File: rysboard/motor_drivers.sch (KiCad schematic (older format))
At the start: 36 parts, among them J2 Motor L, J3 Motor R, Q11 NST847BDP6T5G, Q8 DMP3036SSD-13, U1 L6470, U2 L6470, U5 74HC2G00

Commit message: fixed some bugs. Input protection done. Started implementing 5V Regulator
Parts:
- renumbered Q11 to Q3, Q8 to Q5
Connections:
- net GND: now also Q3.4 (E2); no longer Q3.1 (E1)
- net at R68.1: now also Q3.5 (B2); no longer Q3.2 (B1)
- net at Q5.4 (G2), R69.2: now also Q3.3 (C2); no longer Q3.6 (C1)
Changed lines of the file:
@@
 Connection ~ 3850 950
 $Comp
-L rysboard:NST847BDP6T5G Q11
-U 1 1 603A44DC
+L rysboard:NST847BDP6T5G Q3
+U 2 1 603A44DC
 P 2400 1450
-F 0 "Q11" H 2590 1496 50  0000 L CNN
+F 0 "Q3" H 2590 1496 50  0000 L CNN
 F 1 "NST847BDP6T5G" H 2590 1405 50  0000 L CNN
 F 2 "Package_TO_SOT_SMD:SOT-963" H 2600 1550 50  0001 C CNN
 F 3 "~" H 2400 1450 50  0001 C CNN
-	1    2400 1450
+	2    2400 1450
 	1    0    0    -1
 $EndComp
@@
 $EndComp
 $Comp
-L rysboard:DMP3036SSD-13 Q8
+L rysboard:DMP3036SSD-13 Q5
 U 2 1 6053F608
 P 2900 1050
-F 0 "Q8" V 3242 1050 50  0000 C CNN
+F 0 "Q5" V 3242 1050 50  0000 C CNN
 F 1 "DMP3036SSD-13" V 3151 1050 50  0000 C CNN
 F 2 "Package_SO:SO-8_3.9x4.9mm_P1.27mm" H 3100 975 50  0001 L CIN

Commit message: 3,3Vreg added. MCU first placement
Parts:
- added R30: 0R, Resistor_SMD:R_2512_6332Metric, symbol Device:R
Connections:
- net Vdrive: now also R30.1, R30.2
- net +BATT renamed +12V
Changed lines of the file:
@@
 MOT_EN
-$Comp
-L power:+BATT #PWR062
-U 1 1 6042D379
-P 2200 950
-F 0 "#PWR062" H 2200 800 50  0001 C CNN
-F 1 "+BATT" H 2215 1123 50  0000 C CNN
-F 2 "" H 2200 950 50  0001 C CNN
-F 3 "" H 2200 950 50  0001 C CNN
-	1    2200 950
-	1    0    0    -1
-$EndComp
 $Comp
 L power:GND #PWR063
@@
 	0    1    -1   0
 $EndComp
+$Comp
+L power:+12V #PWR0107
+U 1 1 606DB231
+P 2200 950
+F 0 "#PWR0107" H 2200 800 50  0001 C CNN
+F 1 "+12V" H 2215 1123 50  0000 C CNN
+F 2 "" H 2200 950 50  0001 C CNN
+F 3 "" H 2200 950 50  0001 C CNN
+	1    2200 950
+	1    0    0    -1
+$EndComp
+$Comp
+L Device:R R30
+U 1 1 606E744F
+P 5075 1100
+F 0 "R30" V 4868 1100 50  0000 C CNN
+F 1 "0R" V 4959 1100 50  0000 C CNN
+F 2 "Resistor_SMD:R_2512_6332Metric" V 5005 1100 50  0001 C CNN
+F 3 "~" H 5075 1100 50  0001 C CNN
+	1    5075 1100
+	0    1    1    0
+$EndComp
+$Comp
+L power:Vdrive #PWR0113
+U 1 1 606E7A92
+P 4925 1100
+F 0 "#PWR0113" H 4725 950 50  0001 C CNN
+F 1 "Vdrive" H 4925 1275 50  0000 C CNN
+F 2 "" H 4925 1100 50  0001 C CNN
+F 3 "" H 4925 1100 50  0001 C CNN
+	1    4925 1100
+	1    0    0    -1
+$EndComp
+$Comp
+L power:Vdrive #PWR0114
+U 1 1 606E7D67
+P 5225 1100
+F 0 "#PWR0114" H 5025 950 50  0001 C CNN
+F 1 "Vdrive" H 5225 1275 50  0000 C CNN
+F 2 "" H 5225 1100 50  0001 C CNN
+F 3 "" H 5225 1100 50  0001 C CNN
+	1    5225 1100
+	1    0    0    -1
+$EndComp
 $EndSCHEMATC

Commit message: Bom finished pcb cleanup started
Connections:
- net +3V3: no longer R1.1
- net GND: now also R1.1
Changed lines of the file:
@@
 Wire Wire Line
 	1775 5975 2075 5975
-Connection ~ 1775 5975
-Wire Wire Line
-	1475 5975 1775 5975
 $Comp
 L Device:R R26
@@
 	1    0    0    -1
 $EndComp
+$Comp
+L power:GND #PWR026
+U 1 1 60A36D3D
+P 1475 5975
+F 0 "#PWR026" H 1475 5725 50  0001 C CNN
+F 1 "GND" H 1480 5802 50  0000 C CNN
+F 2 "" H 1475 5975 50  0001 C CNN
+F 3 "" H 1475 5975 50  0001 C CNN
+	1    1475 5975
+	-1   0    0    1
+$EndComp
 $EndSCHEMATC

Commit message: bom + excel ready
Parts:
- R68: value 10KR -> 10k1%
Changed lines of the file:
@@
 P 2050 1450
 F 0 "R68" V 1843 1450 50  0000 C CNN
-F 1 "10KR" V 1934 1450 50  0000 C CNN
+F 1 "10k1%" V 1934 1450 50  0000 C CNN
 F 2 "Resistor_SMD:R_0603_1608Metric" V 1980 1450 50  0001 C CNN
 F 3 "~" H 2050 1450 50  0001 C CNN

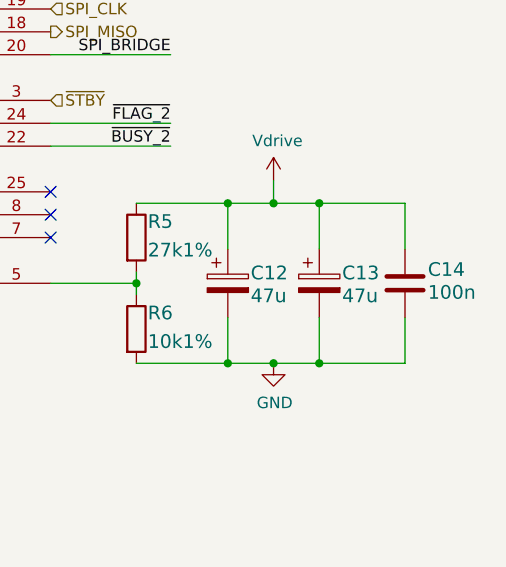
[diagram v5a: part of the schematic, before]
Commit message: some acid pits fixed some ground problems fixed
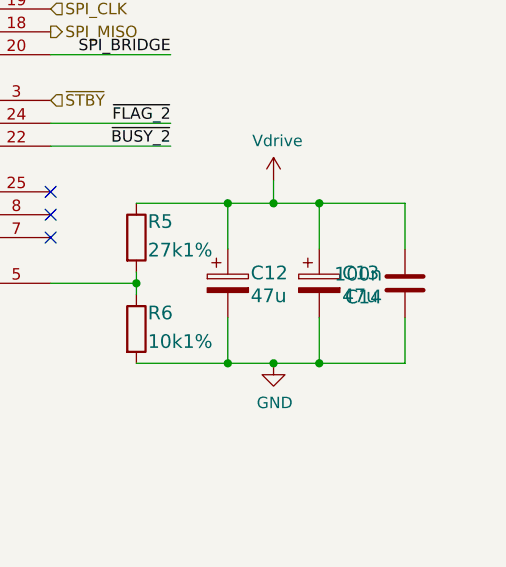
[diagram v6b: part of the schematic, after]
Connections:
- net GND: now also C14.1; no longer C14.2
- net Vdrive: now also C14.2; no longer C14.1
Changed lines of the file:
@@
 F 3 "~" H 10000 3990 60  0001 C CNN
 	1    10100 3900
-	1    0    0    -1
+	-1   0    0    1
 $EndComp
 Wire Wire Line
